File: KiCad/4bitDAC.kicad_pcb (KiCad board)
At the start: 2 copper layers, 12 parts, among them P1 CONN_01X04, P2 CONN_01X04, U1 LM741

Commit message: In process of editing PCB.
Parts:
- R1: value 20k -> 16k
- R2: value 10k -> 16k
- R5: value 20k -> 10k
- R7, R8: value 16k -> 20k
- moved R3 45.0 mm to (121.9, 70.9)
- moved R4 44.9 mm to (121.8, 75.9)
- moved R6 43.6 mm to (154.5, 70.8)
- moved R8 43.6 mm to (154.1, 79.0)
- moved R7 43.6 mm to (154.5, 74.9)
- moved R1 43.5 mm to (137.7, 66.0), turned to 180 degrees
- moved R2 43.3 mm to (137.7, 71.1), turned to 180 degrees
- moved P1 34.6 mm to (167.2, 72.6)
- moved P2 30.9 mm to (110.4, 72.6)
- moved R5 30.2 mm to (121.9, 81.0)
- moved U1 22.2 mm to (133.9, 75.7)
- moved RV1 4.08 mm to (135.0, 91.1), turned to 90 degrees
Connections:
- P1 pad 1: Net-(P1-Pad1) -> Vo
- P1 pad 2: Net-(P1-Pad2) -> V+
- P1 pad 3: Net-(P1-Pad3) -> V-
- P1 pad 4: Net-(P1-Pad4) -> Earth
- P2 pad 1: Vo -> /D0
- P2 pad 2: V+ -> /D1
- P2 pad 3: V- -> /D2
- P2 pad 4: Earth -> /D3
- R1 pad 1: Net-(R1-Pad1) -> Vo
- R1 pad 2: Net-(P1-Pad1) -> Net-(R1-Pad2)
- R2 pad 1: Net-(R2-Pad1) -> Vo
- R2 pad 2: Net-(P1-Pad4) -> Net-(R1-Pad2)
- R3 pad 1: Net-(R2-Pad1) -> Net-(R1-Pad2)
- R3 pad 2: Net-(P1-Pad4) -> /D3
- R4 pad 1: Net-(R2-Pad1) -> Net-(R1-Pad2)
- R4 pad 2: Net-(P1-Pad3) -> /D3
- R5 pad 1: Net-(R2-Pad1) -> Net-(R1-Pad2)
- R5 pad 2: Net-(P1-Pad2) -> /D2
- R6 pad 1: Net-(R2-Pad1) -> Net-(R1-Pad2)
- R6 pad 2: Net-(R1-Pad1) -> /D1
- R7 pad 1: Vo -> Net-(R7-Pad1)
- R7 pad 2: Net-(R2-Pad1) -> /D0
- R8 pad 1: Vo -> Net-(R1-Pad2)
- R8 pad 2: Net-(R2-Pad1) -> Net-(R7-Pad1)
- U1 pad 2: Net-(R2-Pad1) -> Net-(R1-Pad2)
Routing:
- net Net-(R1-Pad2): track 0.00 -> 23.2 mm
- net Vo: track 0.00 -> 10.2 mm
- net Net-(R7-Pad1): track 0.00 -> 5.18 mm
- net /D3: track 0.00 -> 5.18 mm
- net /D2: track 0.00 -> 2.59 mm
- net /D1: track 0.00 -> 2.59 mm
- net /D0: track 0.00 -> 2.59 mm

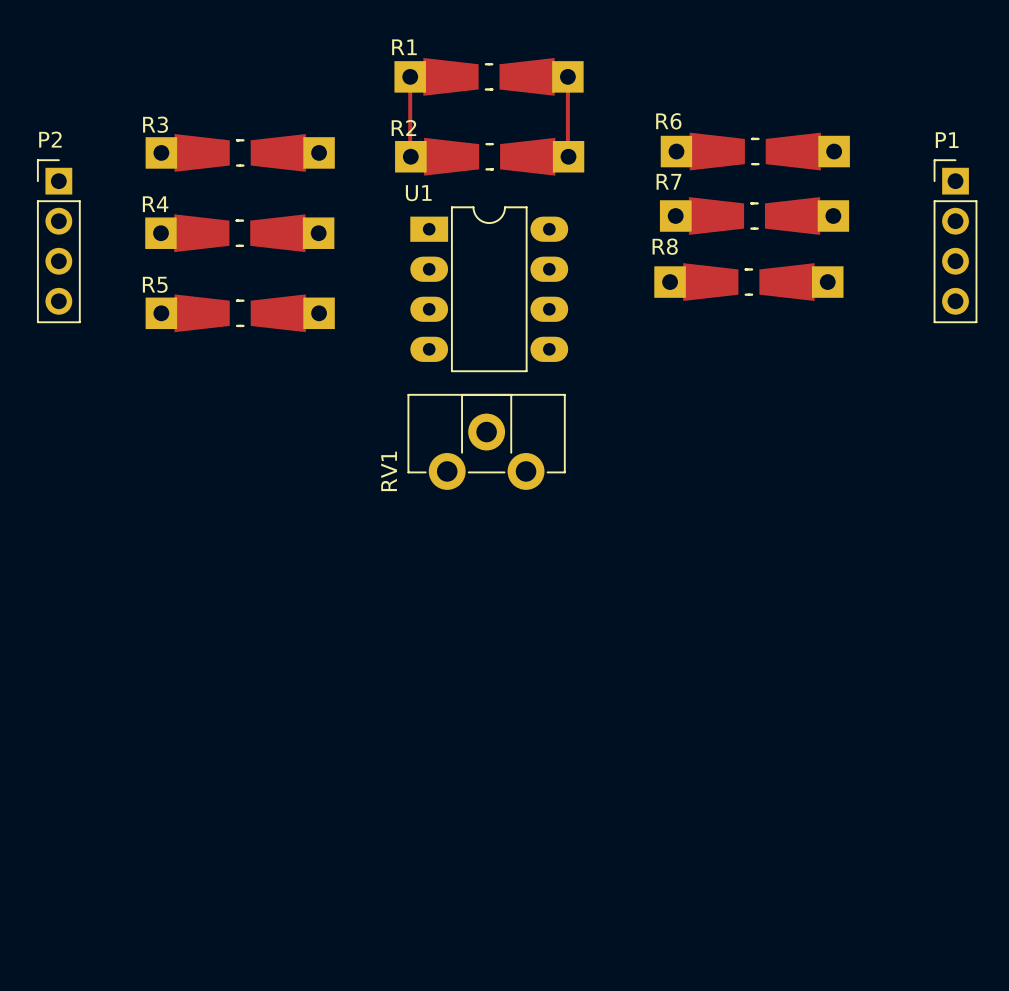
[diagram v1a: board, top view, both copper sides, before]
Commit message: Finalized PCB, added gerbers and drill files, added schematic pdf.
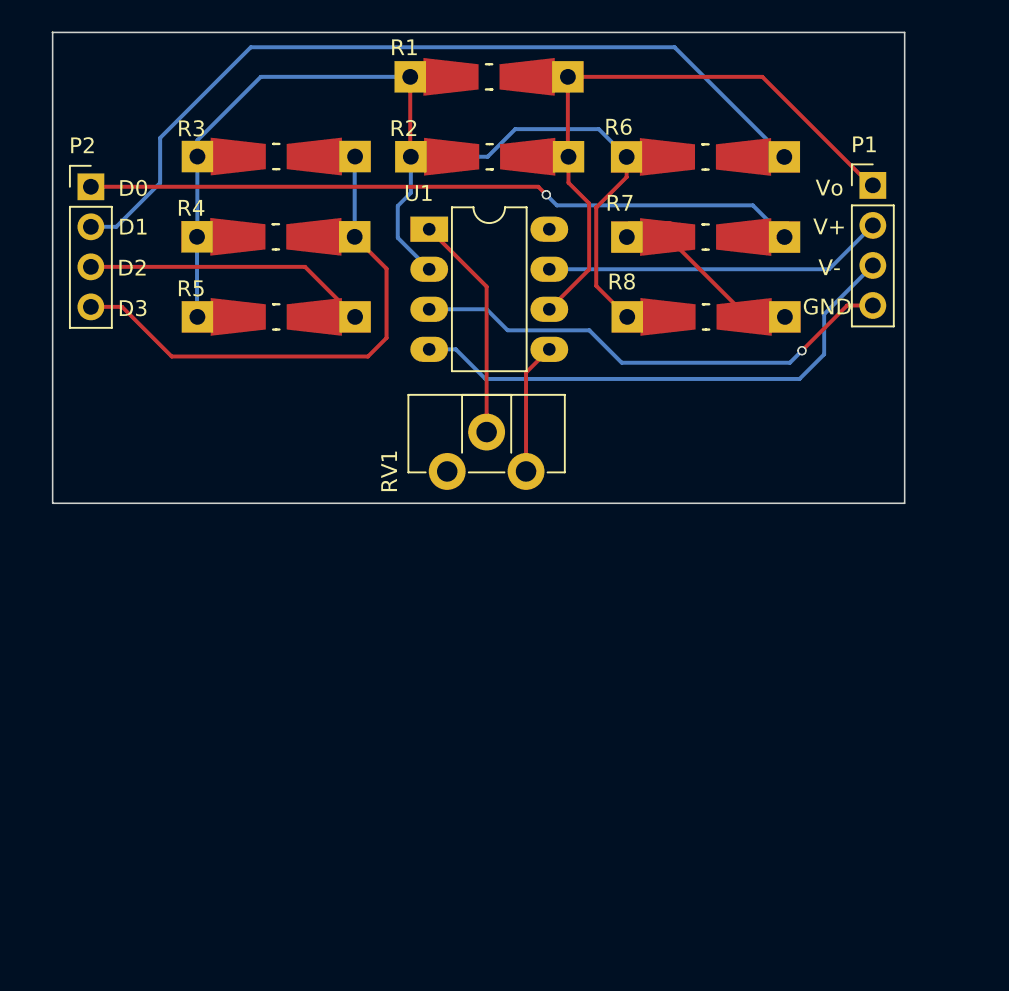
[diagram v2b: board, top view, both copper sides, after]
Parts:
- added logo: , logo:logo, B.Cu at (129.4, 86.0)
- moved P1 5.25 mm to (162.0, 72.9)
- moved R8 3.50 mm to (151.4, 81.3)
- moved R7 3.37 mm to (151.4, 76.2)
- moved R6 3.18 mm to (151.4, 71.1)
- moved R4 2.30 mm to (124.1, 76.2)
- moved R3 2.30 mm to (124.2, 71.1)
- moved R5 2.30 mm to (124.2, 81.3)
- moved P2 2.06 mm to (112.4, 73.0)
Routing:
- net Net-(R1-Pad2): track 23.2 -> 84.8 mm
- net /D1: track 2.59 -> 55.9 mm
- net /D0: track 2.59 -> 47.9 mm, vias 0 -> 1
- net Vo: track 10.2 -> 43.6 mm
- net V-: track 0.00 -> 33.4 mm
- net /D3: track 5.18 -> 38.1 mm
- net Earth: track 0.00 -> 31.1 mm, vias 0 -> 1
- net V+: track 0.00 -> 21.7 mm
- net /D2: track 2.59 -> 20.7 mm
- net Net-(RV1-Pad2): track 0.00 -> 14.4 mm
- net Net-(R7-Pad1): track 5.18 -> 14.7 mm
- net Net-(RV1-Pad3): track 0.00 -> 8.36 mm
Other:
- board outline added: 54.1 x 29.9 mm
- board text added: "D0"
- board text added: "D1"
- board text added: "D2"
- board text added: "D3"
- board text added: "GND"
- board text added: "V+"
- board text added: "V-"
- board text added: "Vo"
